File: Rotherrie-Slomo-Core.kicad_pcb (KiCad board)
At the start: 2 copper layers, 99.6 x 19.4 mm, 43 parts, among them J1 CONN_02X05, J2 JACK_2P, J3 JACK_2P, J4 JACK_2P, J5 JACK_2P, U1 TL074, U2 TL074

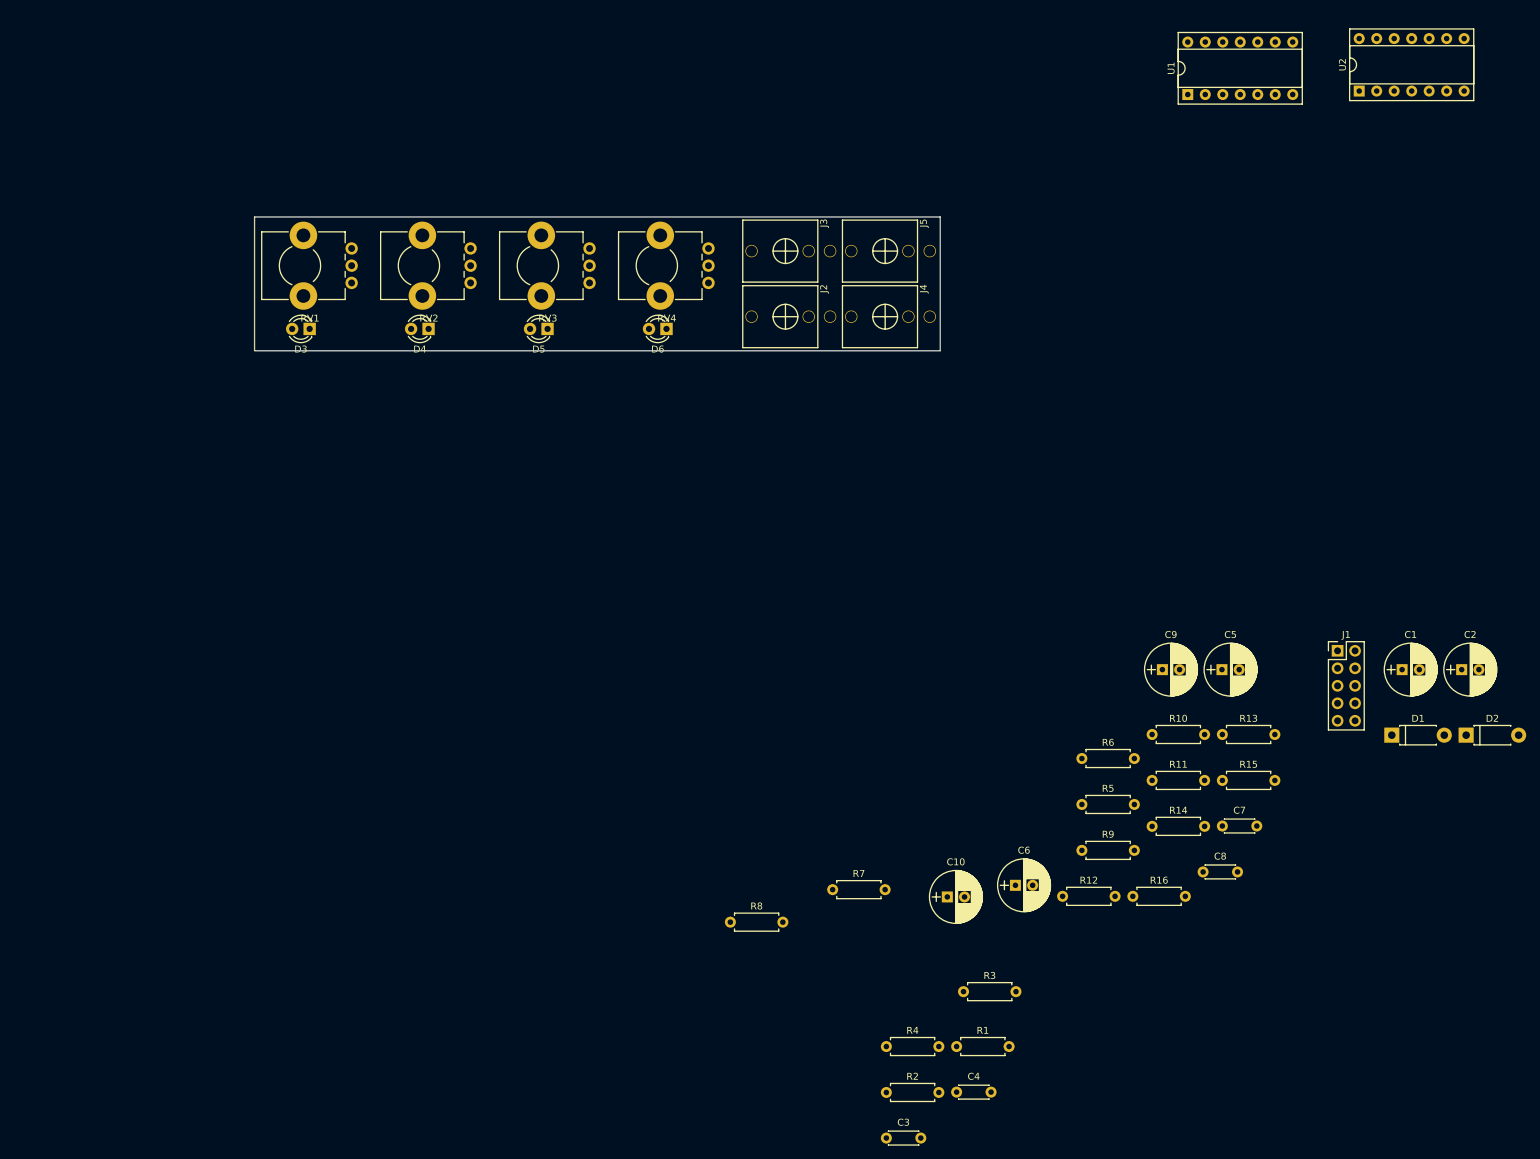
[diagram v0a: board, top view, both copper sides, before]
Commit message: Core board first setup
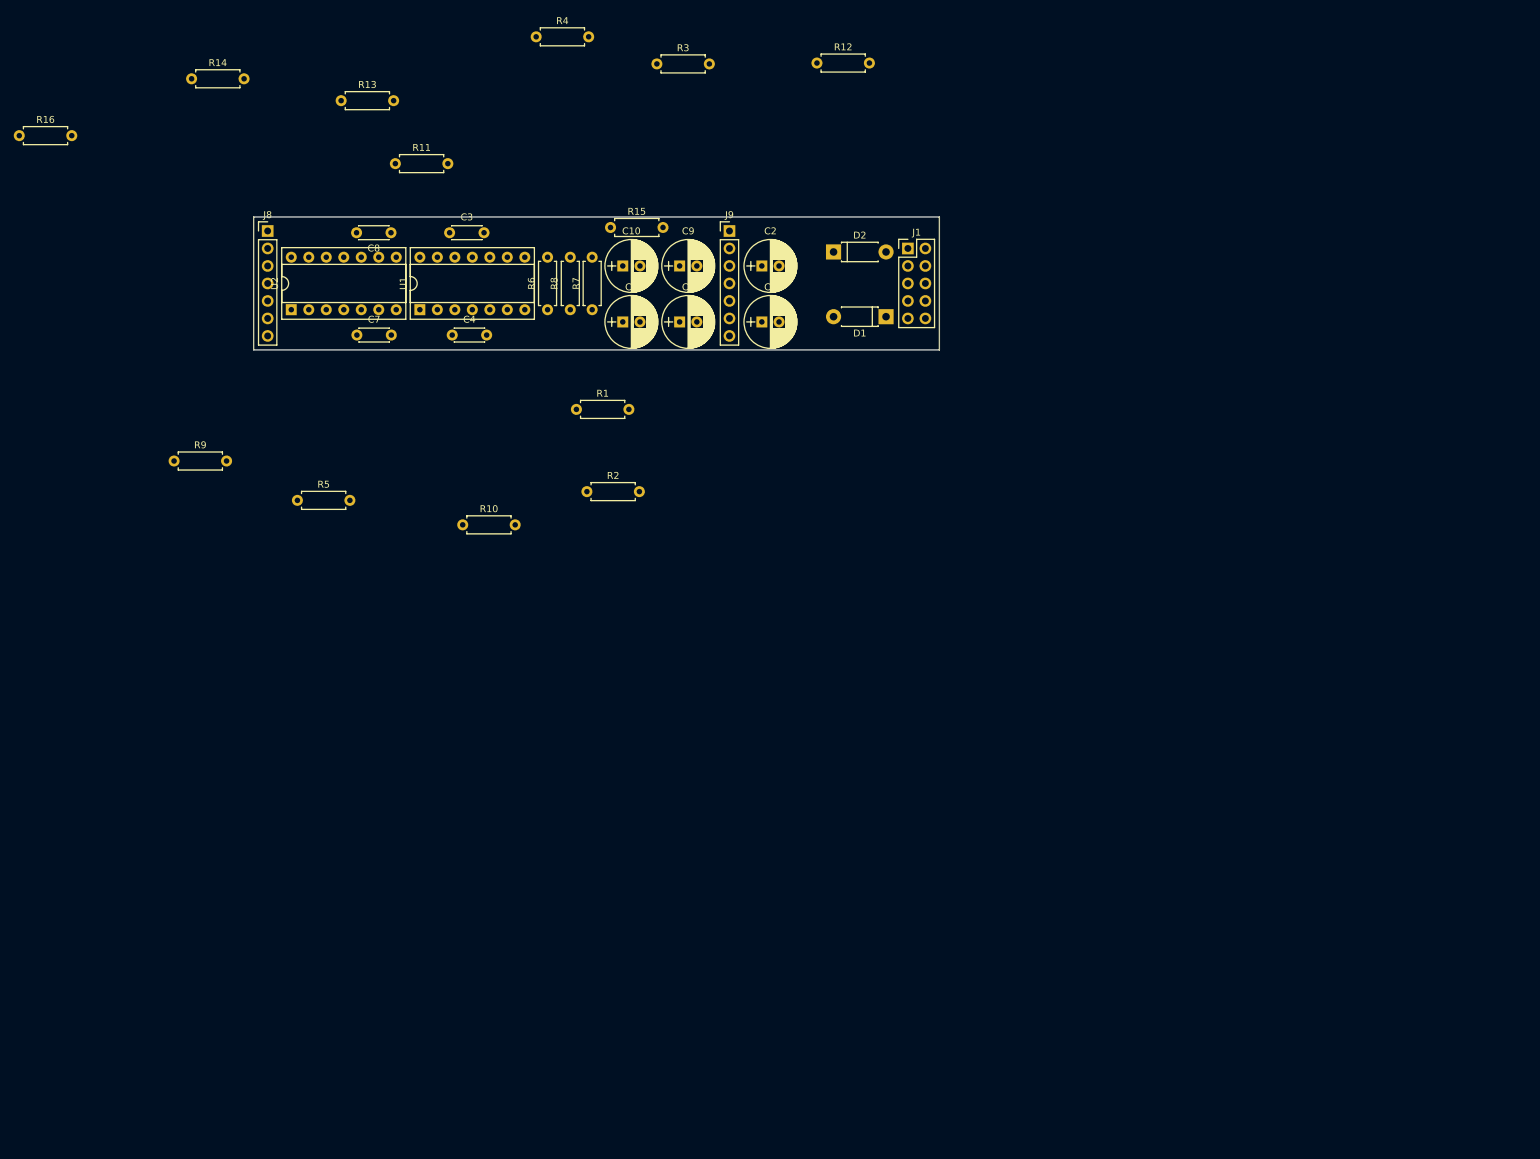
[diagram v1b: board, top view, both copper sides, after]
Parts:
- removed D3, D4, D5, D6: LED_Dual_2pin, LEDs:LED_D3.0mm
- removed J2, J3, J4, J5: JACK_2P, Eurocad:PJ301M-12
- removed RV1, RV2, RV3, RV4: 500k, Potentiometers:Potentiometer_Bourns_PTV09A-1_Horizontal
- added J8: CONN_01X07, Pin_Headers:Pin_Header_Straight_1x07_Pitch2.54mm, F.Cu at (83.3, 50.3)
- added J9: CONN_01X07, Pin_Headers:Pin_Header_Straight_1x07_Pitch2.54mm, F.Cu at (150.4, 50.3)
- moved R16 195.8 mm to (47.2, 36.4)
- moved R14 176.7 mm to (72.3, 28.2)
- moved U2 158.3 mm to (86.7, 61.7)
- moved R13 157.6 mm to (94.0, 31.4)
- moved R4 155.2 mm to (122.3, 22.1)
- moved C8 150.1 mm to (101.2, 50.5), turned to 180 degrees
- moved C3 146.0 mm to (109.7, 50.5)
- moved C7 144.5 mm to (96.3, 65.4)
- moved R9 143.4 mm to (69.7, 83.7)
- moved R3 141.9 mm to (139.8, 26.0)
- moved R11 141.8 mm to (101.9, 40.5)
- moved C4 132.1 mm to (110.1, 65.4)
- moved R12 126.1 mm to (163.1, 25.9)
- moved R5 122.2 mm to (87.6, 89.4)
- moved R15 119.7 mm to (133.1, 49.8)
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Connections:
- net Net-(D3-Pad2) renamed LED1R
- net Net-(D4-Pad2) renamed LED2R
- net Net-(D5-Pad2) renamed LED3R
- net Net-(D6-Pad2) renamed LED4R
- R12 pad 2: Net-(R12-Pad2) -> POT3
- R15 pad 2: Net-(R15-Pad2) -> POT4
- R7 pad 2: Net-(R7-Pad2) -> POT1
- R8 pad 2: Net-(R8-Pad2) -> POT2
- U1 pad 1: Net-(D3-Pad1) -> LED1
- U1 pad 14: Net-(D6-Pad1) -> LED4
- U1 pad 7: Net-(D4-Pad1) -> LED2
- U1 pad 8: Net-(D5-Pad1) -> LED3
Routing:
- net LED3: track 0.00 -> 0.51 mm
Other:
- board size 99.6 x 19.4 mm -> 99.6 x 19.3 mm

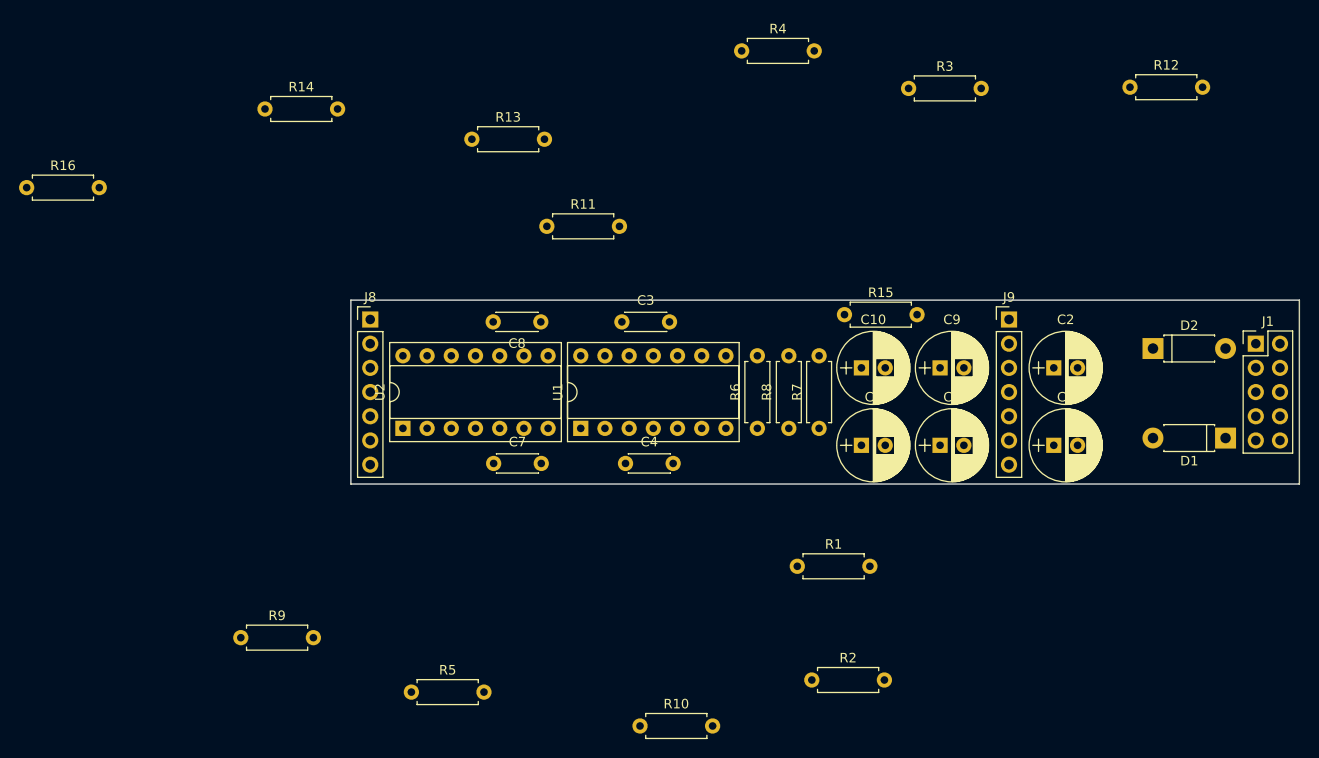
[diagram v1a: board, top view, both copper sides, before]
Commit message: Core board component layout
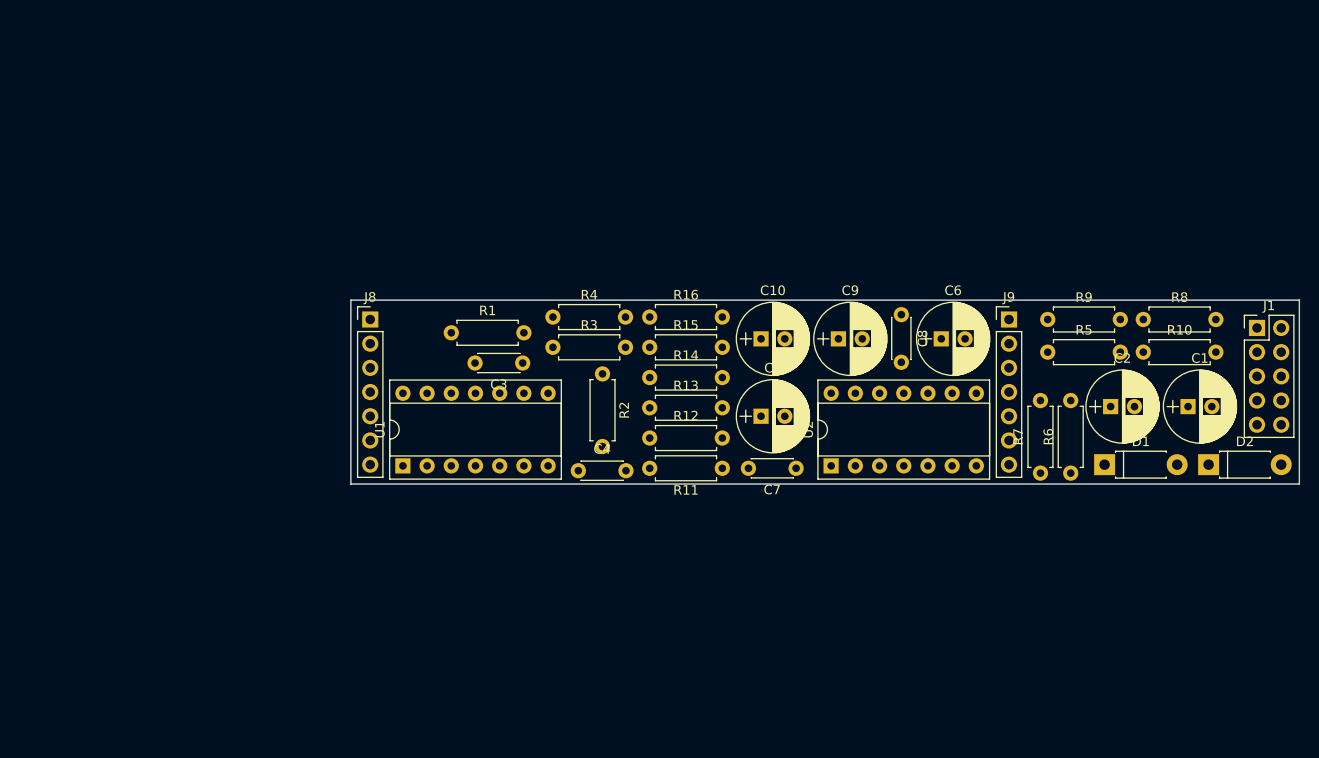
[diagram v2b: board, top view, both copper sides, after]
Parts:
- moved R9 91.1 mm to (154.4, 50.3)
- moved R5 75.7 mm to (154.4, 53.7)
- moved R16 66.8 mm to (112.6, 50.0)
- moved R10 65.8 mm to (164.5, 53.7)
- moved R12 62.4 mm to (112.6, 62.7)
- moved R14 49.3 mm to (112.6, 56.4)
- moved R3 46.2 mm to (102.5, 53.2)
- moved U2 45.1 mm to (131.7, 65.7)
- moved R1 43.8 mm to (91.8, 51.7)
- moved R8 38.9 mm to (164.5, 50.3), turned to 0 degrees
- moved R2 38.9 mm to (107.7, 56.0), turned to 270 degrees
- moved C8 37.9 mm to (139.1, 49.8), turned to 270 degrees
- moved R4 34.3 mm to (102.5, 50.0)
- moved R13 33.8 mm to (112.6, 59.6)
- moved R6 33.2 mm to (156.8, 66.4)
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
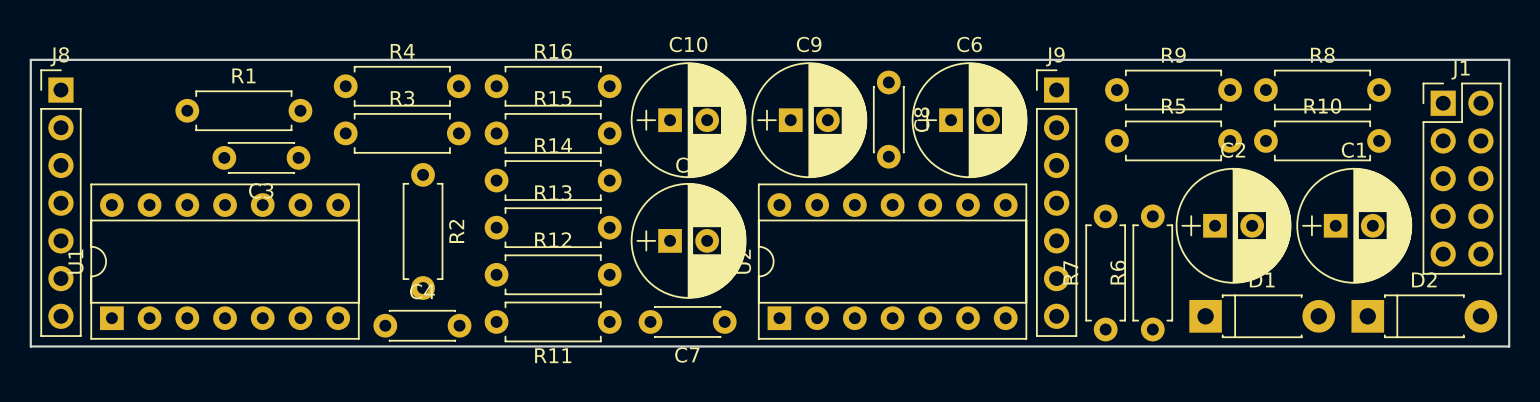
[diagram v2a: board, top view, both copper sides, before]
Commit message: Trouble routing core board. Redesign of header pins needed
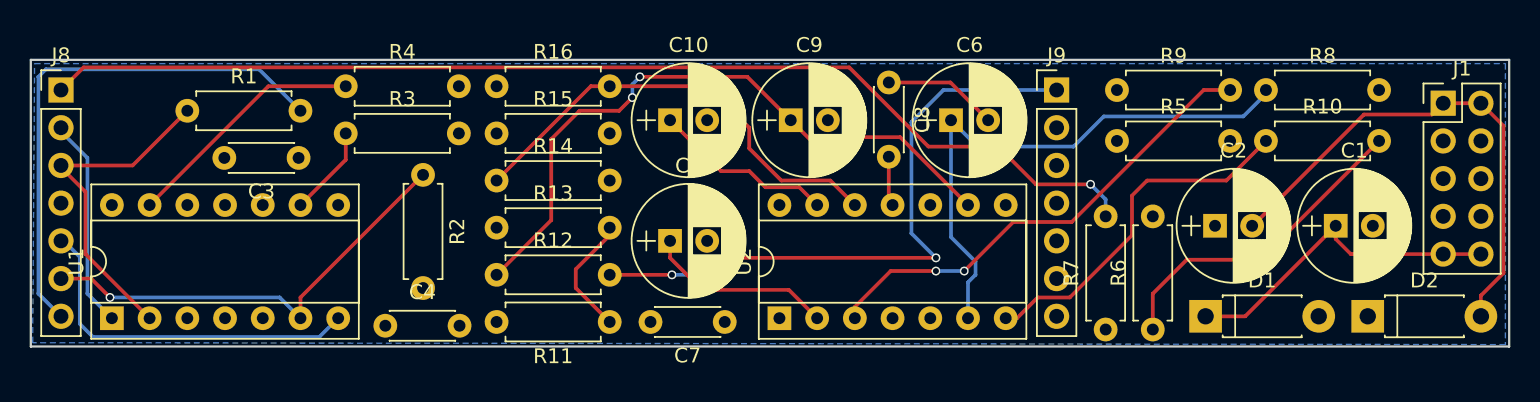
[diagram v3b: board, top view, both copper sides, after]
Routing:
- net POT1: track 0.00 -> 75.8 mm, vias 0 -> 1
- net Net-(C9-Pad1): track 0.00 -> 45.1 mm, vias 0 -> 2
- net GND: track 0.00 -> 43.5 mm
- net POT3: track 0.00 -> 42.9 mm, vias 0 -> 3
- net Net-(C6-Pad1): track 0.00 -> 37.9 mm
- net VEE: track 0.00 -> 37.8 mm
- net Net-(R5-Pad1): track 0.00 -> 32.1 mm, vias 0 -> 2
- net Net-(R14-Pad1): track 0.00 -> 30.9 mm
- net LED2R: track 0.00 -> 30.3 mm, vias 0 -> 1
- net LED2: track 0.00 -> 24.5 mm
- net Net-(R10-Pad1): track 0.00 -> 24.0 mm
- net LED1R: track 0.00 -> 22.8 mm
- net VCC: track 0.00 -> 22.4 mm
- net Net-(R10-Pad2): track 0.00 -> 21.9 mm
- net LED4R: track 0.00 -> 16.5 mm
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- added copper zone on B.Cu, net GND
